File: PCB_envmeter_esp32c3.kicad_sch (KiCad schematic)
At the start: 31 parts, among them J1 USB_C_Receptacle_USB2.0_16P, J3 AE-BME680, J4 SSD1306, Q1 2SC2001, SW1 Reset, SW2 Mode, U1 ESP32-C3-WROOM-02, U2 AP7333-33SAG, U3 NJM2845DL1-33

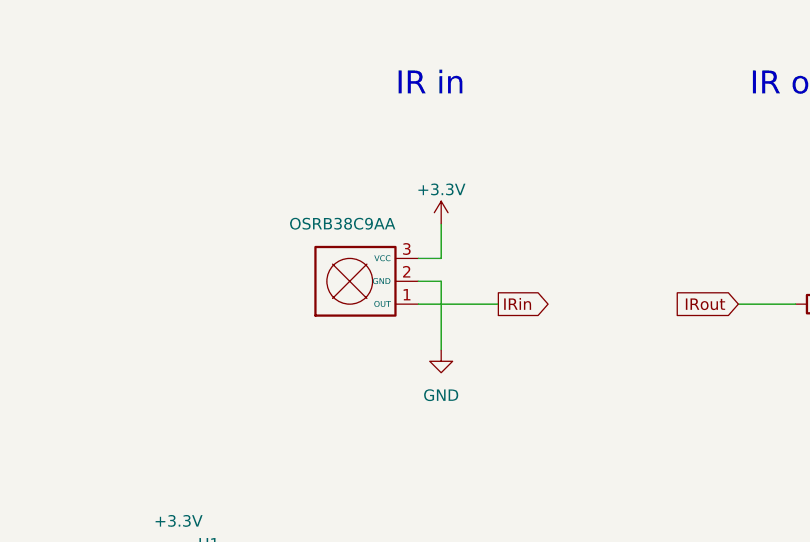
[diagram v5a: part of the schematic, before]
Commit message: Replace OSRB38C9AA symbol
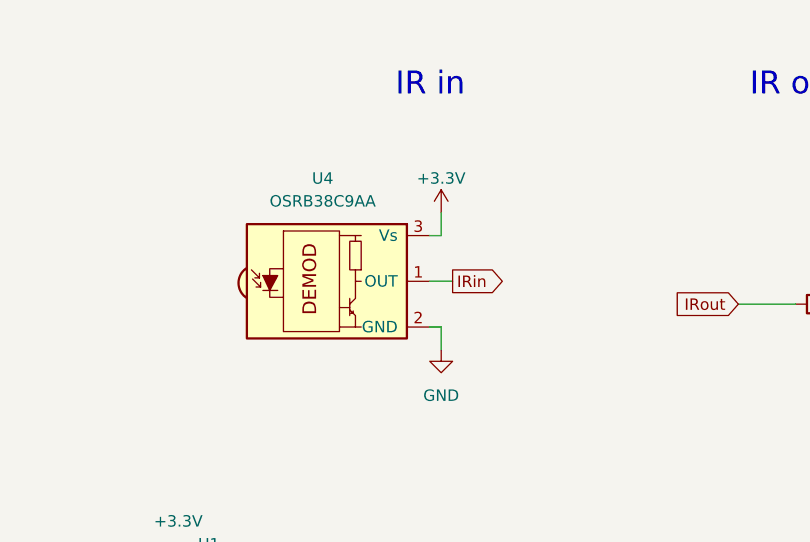
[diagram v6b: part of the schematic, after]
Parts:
- removed IRM1: OSRB38C9AA, OptoDevice:Vishay_MINICAST-3Pin, symbol mylib:OSRB38C9AA
- added U4: OSRB38C9AA, OptoDevice:Vishay_MOLD-3Pin, symbol Interface_Optical:TSOP34S40F
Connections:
- net +3.3V: now also U4.3 (Vs)
- net GND: now also U4.2 (GND)
- net IRin: now also U4.1 (OUT)
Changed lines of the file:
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@@
   (title_block
     (title "IoT環境メーター / スマートリモコン")
-    (date "2024-02-29")
+    (date "2024-03-02")
     (rev "2")
     (company "K.Takata")
@@
     (stroke (width 0) (type default))
   )
+  (wire (pts (xy 201.93 48.26) (xy 201.93 50.8))
+    (stroke (width 0) (type default))
+  )
   (wire (pts (xy 129.54 80.01) (xy 144.78 80.01))
     (stroke (width 0) (type default))
@@
     (stroke (width 0) (type default))
   )
+  (wire (pts (xy 201.93 38.1) (xy 200.66 38.1))
+    (stroke (width 0) (type default))
+  )
   (wire (pts (xy 57.15 99.06) (xy 57.15 101.6))
     (stroke (width 0) (type default))
@@
     (stroke (width 0) (type default))
   )
-  (wire (pts (xy 199.39 45.72) (xy 208.28 45.72))
-    (stroke (width 0) (type default))
-  )
   (wire (pts (xy 111.76 143.51) (xy 114.3 143.51))
     (stroke (width 0) (type default))
@@
     (stroke (width 0) (type default))
   )
-  (wire (pts (xy 201.93 43.18) (xy 199.39 43.18))
-    (stroke (width 0) (type default))
-  )
   (wire (pts (xy 200.66 102.87) (xy 227.33 102.87))
     (stroke (width 0) (type default))
@@
     (stroke (width 0) (type default))
   )
-  (wire (pts (xy 201.93 40.64) (xy 201.93 36.83))
-    (stroke (width 0) (type default))
-  )
   (wire (pts (xy 110.49 24.13) (xy 110.49 22.86))
     (stroke (width 0) (type default))
   )
-  (wire (pts (xy 199.39 40.64) (xy 201.93 40.64))
-    (stroke (width 0) (type default))
-  )
   (wire (pts (xy 111.76 167.64) (xy 114.3 167.64))
     (stroke (width 0) (type default))
@@
     (stroke (width 0) (type default))
   )
-  (wire (pts (xy 201.93 50.8) (xy 201.93 43.18))
-    (stroke (width 0) (type default))
-  )
   (wire (pts (xy 59.69 64.77) (xy 59.69 66.04))
     (stroke (width 0) (type default))
@@
     (stroke (width 0) (type default))
   )
+  (wire (pts (xy 203.2 43.18) (xy 200.66 43.18))
+    (stroke (width 0) (type default))
+  )
   (wire (pts (xy 111.76 170.18) (xy 114.3 170.18))
     (stroke (width 0) (type default))
@@
     (stroke (width 0) (type default))
   )
+  (wire (pts (xy 200.66 48.26) (xy 201.93 48.26))
+    (stroke (width 0) (type default))
+  )
   (wire (pts (xy 200.66 107.95) (xy 227.33 107.95))
     (stroke (width 0) (type default))
   )
   (wire (pts (xy 264.16 50.8) (xy 264.16 62.23))
+    (stroke (width 0) (type default))
+  )
+  (wire (pts (xy 201.93 38.1) (xy 201.93 35.56))
     (stroke (width 0) (type default))
   )
@@
     )
   )
-  (global_label "IRin" (shape output) (at 208.28 45.72 0) (fields_autoplaced)
+  (global_label "IRin" (shape output) (at 203.2 43.18 0) (fields_autoplaced)
     (effects (font (size 1.27 1.27)) (justify left))
-    (property "Intersheetrefs" "${INTERSHEET_REFS}" (at 214.8938 45.72 0)
+    (property "Intersheetrefs" "${INTERSHEET_REFS}" (at 209.8138 43.18 0)
       (effects (font (size 1.27 1.27)) (justify left) hide)
     )
@@
     )
   )
+  (symbol (lib_id "Interface_Optical:TSOP34S40F") (at 190.5 43.18 0) (unit 1)
+    (in_bom yes) (on_board yes) (dnp no) (fields_autoplaced)
+    (property "Reference" "U4" (at 188.765 31.75 0)
+      (effects (font (size 1.27 1.27)))
+    )
+    (property "Value" "OSRB38C9AA" (at 188.765 34.29 0)
+      (effects (font (size 1.27 1.27)))
+    )
+    (property "Footprint" "OptoDevice:Vishay_MOLD-3Pin" (at 189.23 52.705 0)
+      (effects (font (size 1.27 1.27)) hide)
+    )
+    (property "Datasheet" "http://www.vishay.com/docs/82669/tsop32s40f.pdf" (at 207.01 35.56 0)
+      (effects (font (size 1.27 1.27)) hide)
+    )
+    (pin "2")
+    (pin "1")
+    (pin "3")
+    (instances
+      (project "PCB_envmeter_esp32c3"
+        (path "/e56fcc30-bb74-4f59-a961-89b735db6e9b"
+          (reference "U4") (unit 1)
+        )
+      )
+    )
+  )
   (symbol (lib_id "power:+3.3V") (at 172.72 74.93 0) (unit 1)
     (in_bom yes) (on_board yes) (dnp no) (fields_autoplaced)
@@
     )
   )
-  (symbol (lib_id "power:+3.3V") (at 201.93 36.83 0) (unit 1)
-    (in_bom yes) (on_board yes) (dnp no) (fields_autoplaced)
-    (property "Reference" "#PWR026" (at 201.93 40.64 0)
-      (effects (font (size 1.27 1.27)) hide)
-    )
-    (property "Value" "+3.3V" (at 201.93 33.02 0)
-      (effects (font (size 1.27 1.27)))
-    )
-    (property "Footprint" "" (at 201.93 36.83 0)
-      (effects (font (size 1.27 1.27)) hide)
-    )
-    (property "Datasheet" "" (at 201.93 36.83 0)
+  (symbol (lib_id "power:+3.3V") (at 201.93 35.56 0) (unit 1)
+    (in_bom yes) (on_board yes) (dnp no) (fields_autoplaced)
+    (property "Reference" "#PWR026" (at 201.93 39.37 0)
+      (effects (font (size 1.27 1.27)) hide)
+    )
+    (property "Value" "+3.3V" (at 201.93 31.75 0)
+      (effects (font (size 1.27 1.27)))
+    )
+    (property "Footprint" "" (at 201.93 35.56 0)
+      (effects (font (size 1.27 1.27)) hide)
+    )
+    (property "Datasheet" "" (at 201.93 35.56 0)
       (effects (font (size 1.27 1.27)) hide)
     )
@@
         )
       )
-    )
-  )
-  (symbol (lib_id "mylib:OSRB38C9AA") (at 191.77 43.18 90) (unit 1)
-    (in_bom yes) (on_board yes) (dnp no)
-    (property "Reference" "IRM1" (at 182.88 48.26 0)
-      (effects (font (size 1.27 1.27)) (justify left) hide)
-    )
-    (property "Value" "OSRB38C9AA" (at 196.85 36.83 90)
-      (effects (font (size 1.27 1.27)) (justify left))
-    )
-    (property "Footprint" "OptoDevice:Vishay_MINICAST-3Pin" (at 191.77 43.18 0)
-      (effects (font (size 1.27 1.27)) hide)
-    )
-    (property "Datasheet" "" (at 191.77 43.18 0)
-      (effects (font (size 1.27 1.27)) hide)
-    )
-    (pin "1")
-    (pin "2")
-    (pin "3")
-    (instances
-      (project "PCB_envmeter_esp32c3"
-        (path "/e56fcc30-bb74-4f59-a961-89b735db6e9b"
-          (reference "IRM1") (unit 1)
-        )
-      )

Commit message: Renumber
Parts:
- renumbered R9 to R8, R8 to R9
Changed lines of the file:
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@@
   (symbol (lib_id "Device:R") (at 264.16 25.4 0) (unit 1)
     (in_bom yes) (on_board yes) (dnp no) (fields_autoplaced)
-    (property "Reference" "R8" (at 266.7 24.13 0)
+    (property "Reference" "R9" (at 266.7 24.13 0)
       (effects (font (size 1.27 1.27)) (justify left))
     )
@@
       (project "PCB_envmeter_esp32c3"
         (path "/e56fcc30-bb74-4f59-a961-89b735db6e9b"
-          (reference "R8") (unit 1)
+          (reference "R9") (unit 1)
         )
       )
@@
       (effects (font (size 1.27 1.27)) hide)
     )
+    (property "Sim.Enable" "0" (at 110.49 49.53 0)
+      (effects (font (size 1.27 1.27)) hide)
+    )
     (pin "1")
     (pin "2")
@@
   (symbol (lib_id "Device:R") (at 252.73 54.61 0) (unit 1)
     (in_bom yes) (on_board yes) (dnp no) (fields_autoplaced)
-    (property "Reference" "R9" (at 255.27 53.975 0)
-      (effects (font (size 1.27 1.27)) (justify left))
-    )
-    (property "Value" "4.7k" (at 255.27 56.515 0)
+    (property "Reference" "R8" (at 255.27 53.34 0)
+      (effects (font (size 1.27 1.27)) (justify left))
+    )
+    (property "Value" "4.7k" (at 255.27 55.88 0)
       (effects (font (size 1.27 1.27)) (justify left))
     )
@@
       (project "PCB_envmeter_esp32c3"
         (path "/e56fcc30-bb74-4f59-a961-89b735db6e9b"
-          (reference "R9") (unit 1)
+          (reference "R8") (unit 1)
         )
       )
@@
       (effects (font (size 1.27 1.27)) hide)
     )
+    (property "Sim.Enable" "0" (at 63.5 68.58 0)
+      (effects (font (size 1.27 1.27)) hide)
+    )
